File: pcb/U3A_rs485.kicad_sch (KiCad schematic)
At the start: 17 parts, among them J1 Screw_Terminal_01x06, J2 Conn_01x07_Socket, J3 Conn_01x02_Pin, J4 Conn_01x08_Socket, J5 Conn_01x02_Pin, U1 THVD1452DR

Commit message: Add vendor-ids to devices
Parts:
- J3, J5: Vendor (none) -> HTL; VendorId (none) -> 101521
- R1, R2: Vendor (none) -> HTL; VendorId (none) -> 102933
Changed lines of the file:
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@@
+      (effects (font (size 1.27 1.27)) hide)
+    )
+    (property "Vendor" "HTL" (at 161.29 96.52 0)
+      (effects (font (size 1.27 1.27)) hide)
+    )
+    (property "VendorId" "102933" (at 161.29 96.52 0)
       (effects (font (size 1.27 1.27)) hide)
     )
@@
       (effects (font (size 1.27 1.27)) hide)
     )
+    (property "Vendor" "HTL" (at 171.45 71.12 0)
+      (effects (font (size 1.27 1.27)) hide)
+    )
+    (property "VendorId" "101521" (at 171.45 71.12 0)
+      (effects (font (size 1.27 1.27)) hide)
+    )
     (pin "2")
     (pin "1")
@@
       (effects (font (size 1.27 1.27)) hide)
     )
+    (property "Vendor" "HTL" (at 171.45 96.52 0)
+      (effects (font (size 1.27 1.27)) hide)
+    )
+    (property "VendorId" "101521" (at 171.45 96.52 0)
+      (effects (font (size 1.27 1.27)) hide)
+    )
     (pin "2")
     (pin "1")
@@
       (effects (font (size 1.27 1.27)) hide)
     )
+    (property "Vendor" "HTL" (at 161.29 71.12 0)
+      (effects (font (size 1.27 1.27)) hide)
+    )
+    (property "VendorId" "102933" (at 161.29 71.12 0)
+      (effects (font (size 1.27 1.27)) hide)
+    )

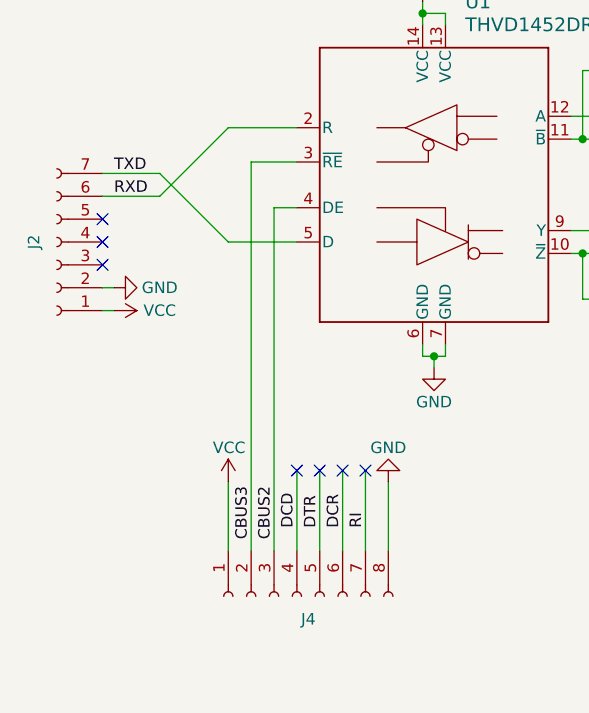
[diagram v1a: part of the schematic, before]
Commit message: Add missing pull-up resistor
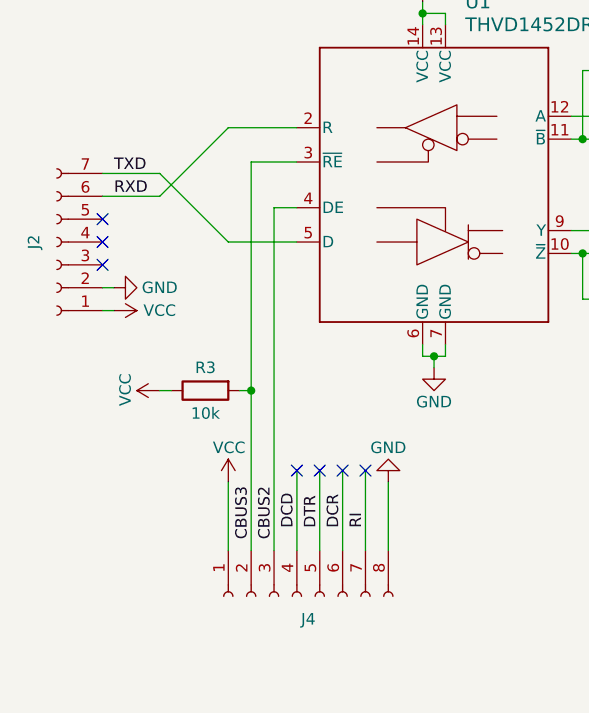
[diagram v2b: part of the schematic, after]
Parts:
- added R3: 10k, Resistor_SMD:R_1206_3216Metric, symbol Device:R
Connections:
- net CBUS3: now also R3.2
- net VCC: now also R3.1
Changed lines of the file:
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@@
   (junction (at 114.3 171.45) (diameter 0) (color 0 0 0 0)
+  )
+  (junction (at 119.38 106.68) (diameter 0) (color 0 0 0 0)
   )
   (junction (at 127 184.15) (diameter 0) (color 0 0 0 0)
@@
     (stroke (width 0) (type default))
   )
+  (wire (pts (xy 119.38 106.68) (xy 119.38 124.46))
+    (stroke (width 0) (type default))
+  )
   (wire (pts (xy 109.22 82.55) (xy 116.84 90.17))
     (stroke (width 0) (type default))
@@
     (stroke (width 0) (type default))
   )
+  (wire (pts (xy 109.22 106.68) (xy 110.49 106.68))
+    (stroke (width 0) (type default))
+  )
   (wire (pts (xy 134.62 124.46) (xy 134.62 116.84))
     (stroke (width 0) (type default))
@@
     (stroke (width 0) (type default))
   )
-  (wire (pts (xy 119.38 81.28) (xy 119.38 124.46))
+  (wire (pts (xy 119.38 81.28) (xy 119.38 106.68))
     (stroke (width 0) (type default))
   )
@@
   )
   (wire (pts (xy 121.92 86.36) (xy 124.46 86.36))
+    (stroke (width 0) (type default))
+  )
+  (wire (pts (xy 118.11 106.68) (xy 119.38 106.68))
     (stroke (width 0) (type default))
   )
@@
         (path "/9334361a-f7a5-4302-90e9-4b89798c8fc6"
           (reference "#PWR010") (unit 1)
+        )
+      )
+    )
+  )
+  (symbol (lib_id "Device:R") (at 114.3 106.68 90) (mirror x) (unit 1)
+    (in_bom yes) (on_board yes) (dnp no)
+    (property "Reference" "R3" (at 114.3 104.14 90)
+      (effects (font (size 1.27 1.27)))
+    )
+    (property "Value" "10k" (at 114.3 109.22 90)
+      (effects (font (size 1.27 1.27)))
+    )
+    (property "Footprint" "Resistor_SMD:R_1206_3216Metric" (at 114.3 104.902 90)
+      (effects (font (size 1.27 1.27)) hide)
+    )
+    (property "Datasheet" "~" (at 114.3 106.68 0)
+      (effects (font (size 1.27 1.27)) hide)
+    )
+    (property "Vendor" "HTL" (at 114.3 106.68 0)
+      (effects (font (size 1.27 1.27)) hide)
+    )
+    (property "VendorId" "102967" (at 114.3 106.68 0)
+      (effects (font (size 1.27 1.27)) hide)
+    )
+    (pin "2")
+    (pin "1")
+    (instances
+      (project "U3A_rs485"
+        (path "/9334361a-f7a5-4302-90e9-4b89798c8fc6"
+          (reference "R3") (unit 1)
         )
       )
@@
         )
       )
+    )
+  )
+  (symbol (lib_id "power:VCC") (at 109.22 106.68 90) (mirror x) (unit 1)
+    (in_bom yes) (on_board yes) (dnp no)
+    (property "Reference" "#PWR013" (at 113.03 106.68 0)
+      (effects (font (size 1.27 1.27)) hide)
+    )
+    (property "Value" "VCC" (at 105.41 104.775 0)
+      (effects (font (size 1.27 1.27)) (justify left))
+    )
+    (property "Footprint" "" (at 109.22 106.68 0)
+      (effects (font (size 1.27 1.27)) hide)
+    )
+    (property "Datasheet" "" (at 109.22 106.68 0)
+      (effects (font (size 1.27 1.27)) hide)
+    )
+    (pin "1")
+    (instances
+      (project "U3A_rs485"
+        (path "/9334361a-f7a5-4302-90e9-4b89798c8fc6"
+          (reference "#PWR013") (unit 1)
+        )
+      )
